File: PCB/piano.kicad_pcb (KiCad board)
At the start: 2 copper layers, 100 x 90 mm, 35 parts, among them J1 Conn_01x02, J2 Conn_01x04, J3 Conn_01x04, SW1 0, SW10 9, SW11 A, SW12 B, SW13 C, SW14 D, SW15 E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

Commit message: v0.2 PCB
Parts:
- added ?: , , F.Cu at (133.7, 64.2)
- added Q1: 2N3904, Package_TO_SOT_THT:TO-92_Inline, F.Cu at (169.4, 51.1)
- added R5: 10k, Resistor_THT:R_Axial_DIN0207_L6.3mm_D2.5mm_P10.16mm_Horizontal, F.Cu at (181.7, 34.6)
- added SW1: SW_SPDT_MSM, Suat:Schiebeschalter, F.Cu at (208.4, 34.0)
- added U2: LiPo_Module, Suat:LiPoChargerModule, F.Cu at (218.3, 49.0)
- BZ1: footprint Buzzer_Beeper:Buzzer_TDK_PS1240P02BT_D12.2mm_H6.5mm -> Suat:Buzzer_D12mm_Pins6mm
- D1, D2, D3, D4: footprint Diode_THT:D_A-405_P10.16mm_Horizontal -> Suat:D_A-405_P10.16mm_Horizontal
- J1: footprint Connector_JST:JST_EH_B2B-EH-A_1x02_P2.50mm_Vertical -> Connector_JST:JST_PH_B2B-PH-K_1x02_P2.00mm_Vertical
- J2, J3: footprint Connector_PinHeader_2.54mm:PinHeader_1x04_P2.54mm_Vertical -> Suat:PinHeader_1x04_P2.54mm_Vertical_Simple
- R1, R2, R3, R4: value R -> 10k
- SW-0: renamed from SW1; value 0 -> 0x0; footprint Button_Switch_THT:SW_PUSH_6mm -> Suat:SW_PUSH_6mm
- SW-1: renamed from SW2; value 1 -> 0x1; footprint Button_Switch_THT:SW_PUSH_6mm -> Suat:SW_PUSH_6mm
- SW-2: renamed from SW3; value 2 -> 0x2; footprint Button_Switch_THT:SW_PUSH_6mm -> Suat:SW_PUSH_6mm
- SW-3: renamed from SW4; value 3 -> 0x3; footprint Button_Switch_THT:SW_PUSH_6mm -> Suat:SW_PUSH_6mm
- SW-4: renamed from SW5; value 4 -> 0x4; footprint Button_Switch_THT:SW_PUSH_6mm -> Suat:SW_PUSH_6mm
- SW-5: renamed from SW6; value 5 -> 0x5; footprint Button_Switch_THT:SW_PUSH_6mm -> Suat:SW_PUSH_6mm
- SW-6: renamed from SW7; value 6 -> 0x6; footprint Button_Switch_THT:SW_PUSH_6mm -> Suat:SW_PUSH_6mm
- SW-7: renamed from SW8; value 7 -> 0x7; footprint Button_Switch_THT:SW_PUSH_6mm -> Suat:SW_PUSH_6mm
- SW-8: renamed from SW9; value 8 -> 0x8; footprint Button_Switch_THT:SW_PUSH_6mm -> Suat:SW_PUSH_6mm
- SW-9: renamed from SW10; value 9 -> 0x9; footprint Button_Switch_THT:SW_PUSH_6mm -> Suat:SW_PUSH_6mm
- SW-A1: renamed from SW11; value A -> 0xA; footprint Button_Switch_THT:SW_PUSH_6mm -> Suat:SW_PUSH_6mm
- SW-B1: renamed from SW12; value B -> 0xB; footprint Button_Switch_THT:SW_PUSH_6mm -> Suat:SW_PUSH_6mm
- SW-C1: renamed from SW13; value C -> 0xC; footprint Button_Switch_THT:SW_PUSH_6mm -> Suat:SW_PUSH_6mm
- SW-D1: renamed from SW14; value D -> 0xD; footprint Button_Switch_THT:SW_PUSH_6mm -> Suat:SW_PUSH_6mm
- SW-E1: renamed from SW15; value E -> 0xE3; footprint Button_Switch_THT:SW_PUSH_6mm -> Suat:SW_PUSH_6mm
- SW-F1: renamed from SW16; value F -> 0xF; footprint Button_Switch_THT:SW_PUSH_6mm -> Suat:SW_PUSH_6mm
- moved D1 65.5 mm to (214.6, 70.7)
- moved D2 47.5 mm to (206.2, 70.7)
- moved BZ1 39.0 mm to (170.0, 39.2)
- moved R4 37.3 mm to (154.3, 70.8), turned to -90 degrees
- moved D3 29.5 mm to (197.9, 70.7)
- moved R3 27.6 mm to (162.5, 70.8), turned to -90 degrees
- moved J1 26.5 mm to (217.0, 35.2)
- moved R2 19.7 mm to (170.7, 70.8), turned to -90 degrees
- moved R1 16.2 mm to (178.8, 70.8), turned to -90 degrees
- moved D4 11.6 mm to (189.5, 70.7)
- moved J2 9.96 mm to (198.2, 52.2), turned to -90 degrees
- moved J3 5.62 mm to (187.0, 40.7)
- moved SW-9 2.09 mm to (165.4, 100.0)
- moved SW-8 1.32 mm to (155.1, 100.0)
- moved SW-A1 1.23 mm to (185.6, 100.0)
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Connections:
- ? pad 1: (no net) -> GND (x4)
- BZ1 pad 1: Net-(BZ1-Pad1) -> Net-(SW1-Pad1)
- BZ1 pad 2: GND -> Net-(BZ1-Pad2)
- J1 pad 1: GND -> Net-(J1-Pad1)
- REF** pad 1: (no net) -> GND (x2)
- U1 pad 3: Net-(BZ1-Pad1) -> Net-(U1-Pad3)
- U1 pad 9: Net-(J1-Pad2) -> Net-(SW1-Pad1)
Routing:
- net Net-(SW1-Pad1): track 0.00 -> 80.1 mm
- net Net-(BZ1-Pad1): track 65.1 -> 0.00 mm
- net Net-(J1-Pad2): track 76.6 -> 18.7 mm
- net Net-(D2-Pad2): track 135.3 -> 181.1 mm, vias 1 -> 0
- net Net-(D1-Pad2): track 144.0 -> 183.9 mm
- net Net-(U1-Pad3): track 0.00 -> 32.7 mm
- net D8: track 213.5 -> 246.2 mm
- net Net-(Q1-Pad2): track 0.00 -> 31.4 mm
- net Net-(D3-Pad2): track 168.8 -> 197.4 mm
- net Net-(SW1-Pad2): track 0.00 -> 24.9 mm
- net GND: track 23.0 -> 0.00 mm, vias 7 -> 0
- net D7: track 200.3 -> 222.7 mm, vias 1 -> 0
- net Net-(J1-Pad1): track 0.00 -> 22.0 mm
- net Net-(BZ1-Pad2): track 0.00 -> 15.6 mm
- net D4: track 78.5 -> 92.3 mm, vias 1 -> 0
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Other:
- board text added: "+ -"
- board text added: "0 4 8 C 1 5 9 D 2 6 A E 3 7 B F"
- board text added: "Cols→"
- board text added: "Rows→"
- board text added: "v0.2 ://sui.li"
- board text removed: "+ - D0"
- board text removed: "F E D C B A 9 8 7 6 5 4 3 2 1 0"
- board text removed: "v0.1 ://sui.li"

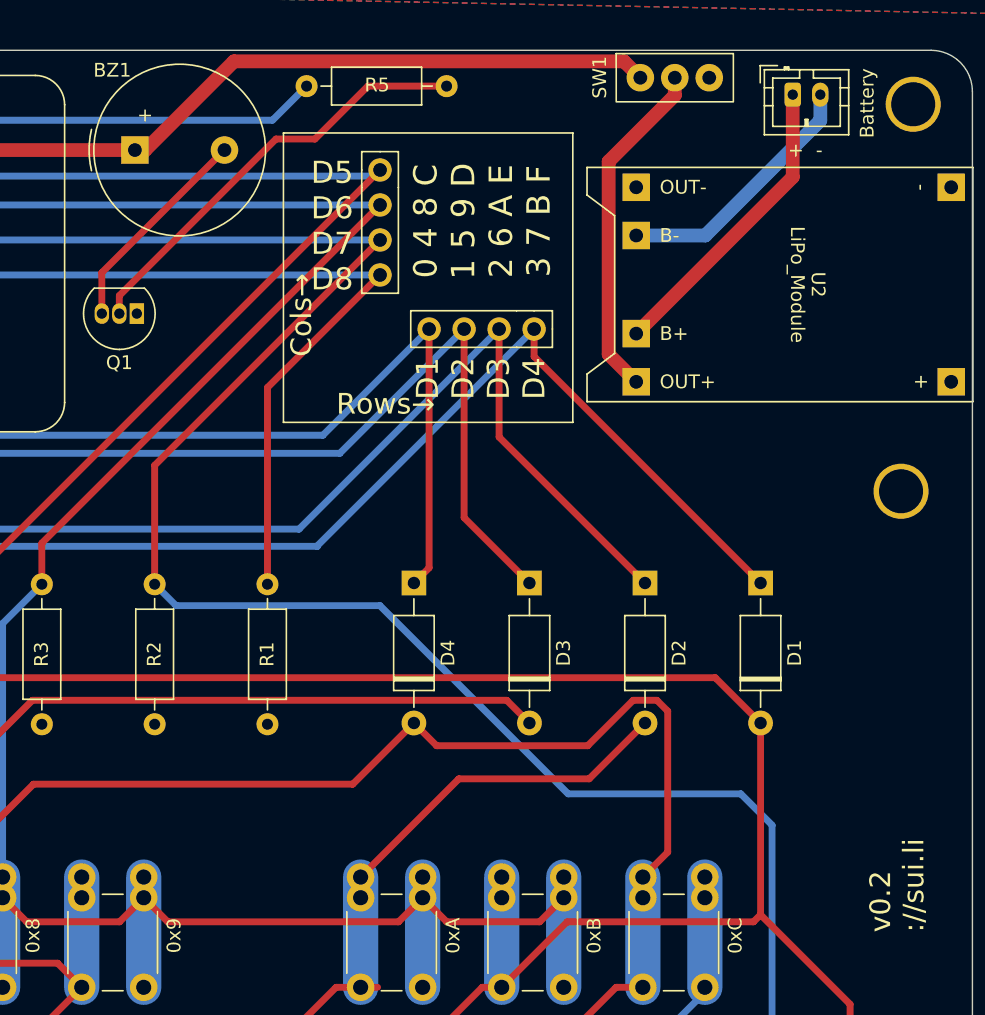
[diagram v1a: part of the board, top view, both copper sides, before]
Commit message: update pcb (larger footprint for transistor)
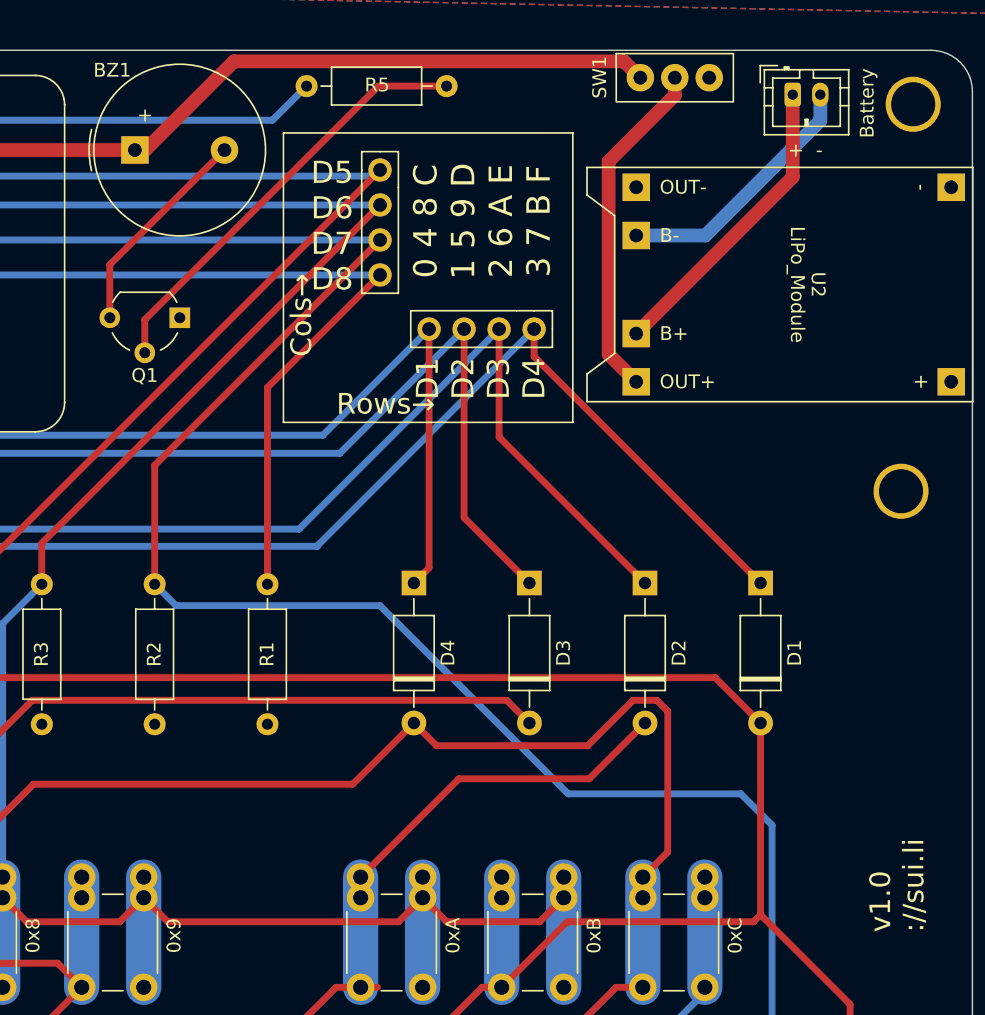
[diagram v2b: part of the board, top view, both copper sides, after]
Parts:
- Q1: footprint Package_TO_SOT_THT:TO-92_Inline -> Package_TO_SOT_THT:TO-92_Wide
- moved Q1 3.13 mm to (172.5, 51.4)
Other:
- board text added: "v1.0 ://sui.li"
- board text removed: "v0.2 ://sui.li"
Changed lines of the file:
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@@
     )
   )
-  (footprint "Package_TO_SOT_THT:TO-92_Inline" (layer "F.Cu")
-    (at 169.36 51.11 180)
-    (descr "TO-92 leads in-line, narrow, oval pads, drill 0.75mm (see NXP sot054_po.pdf)")
+  (footprint "Package_TO_SOT_THT:TO-92_Wide" (layer "F.Cu")
+    (at 172.48 51.41 180)
+    (descr "TO-92 leads molded, wide, drill 0.75mm (see NXP sot054_po.pdf)")
     (tags "to-92 sc-43 sc-43a sot54 PA33 transistor")
     (property "Sheetfile" "piano.kicad_sch")
     (property "Sheetname" "")
     (attr through_hole)
-    (fp_text reference "Q1" (at 1.27 -3.56) (layer "F.SilkS")
-      (effects (font (size 1 1) (thickness 0.15)))
-    )
-    (fp_text value "2N3904" (at 1.27 2.79) (layer "F.Fab")
-      (effects (font (size 1 1) (thickness 0.15)))
-    )
-    (fp_text user "${REFERENCE}" (at 1.27 0) (layer "F.Fab")
-      (effects (font (size 1 1) (thickness 0.15)))
-    )
-    (fp_line (start -0.53 1.85) (end 3.07 1.85) (layer "F.SilkS") (width 0.12))
-    (fp_arc (start -0.568478 1.838478) (mid -1.132087 -0.994977) (end 1.27 -2.6) (layer "F.SilkS") (width 0.12))
-    (fp_arc (start 1.27 -2.6) (mid 3.672087 -0.994977) (end 3.108478 1.838478) (layer "F.SilkS") (width 0.12))
-    (fp_line (start -1.46 -2.73) (end 4 -2.73) (layer "F.CrtYd") (width 0.05))
-    (fp_line (start -1.46 -2.73) (end -1.46 2.01) (layer "F.CrtYd") (width 0.05))
-    (fp_line (start 4 2.01) (end 4 -2.73) (layer "F.CrtYd") (width 0.05))
-    (fp_line (start 4 2.01) (end -1.46 2.01) (layer "F.CrtYd") (width 0.05))
-    (fp_line (start -0.5 1.75) (end 3 1.75) (layer "F.Fab") (width 0.1))
-    (fp_arc (start -0.483625 1.753625) (mid -1.021221 -0.949055) (end 1.27 -2.48) (layer "F.Fab") (width 0.1))
-    (fp_arc (start 1.27 -2.48) (mid 3.561221 -0.949055) (end 3.023625 1.753625) (layer "F.Fab") (width 0.1))
-    (pad "1" thru_hole rect (at 0 0 180) (size 1.05 1.5) (drill 0.75) (layers *.Cu *.Mask)
+    (fp_text reference "Q1" (at 2.55 -4.19 180) (layer "F.SilkS")
+      (effects (font (size 1 1) (thickness 0.15)))
+    )
+    (fp_text value "2N3904" (at 2.54 2.79 180) (layer "F.Fab")
+      (effects (font (size 1 1) (thickness 0.15)))
+    )
+    (fp_text user "${REFERENCE}" (at 2.54 0 180) (layer "F.Fab")
+      (effects (font (size 1 1) (thickness 0.15)))
+    )
+    (fp_line (start 0.74 1.85) (end 4.34 1.85) (layer "F.SilkS") (width 0.12))
+    (fp_arc (start 0.74 1.85) (mid 0.446097 1.509328) (end 0.215816 1.122795) (layer "F.SilkS") (width 0.12))
+    (fp_arc (start 4.864184 1.122795) (mid 4.633903 1.509328) (end 4.34 1.85) (layer "F.SilkS") (width 0.12))
+    (fp_arc (start 0.172801 -1.103842) (mid 0.678995 -1.832692) (end 1.4 -2.35) (layer "F.SilkS") (width 0.12))
+    (fp_arc (start 3.65 -2.35) (mid 4.382279 -1.833196) (end 4.895458 -1.098371) (layer "F.SilkS") (width 0.12))
+    (fp_line (start -1.01 -3.55) (end 6.09 -3.55) (layer "F.CrtYd") (width 0.05))
+    (fp_line (start 6.09 2.01) (end 6.09 -3.55) (layer "F.CrtYd") (width 0.05))
+    (fp_line (start 6.09 2.01) (end -1.01 2.01) (layer "F.CrtYd") (width 0.05))
+    (fp_line (start -1.01 -3.55) (end -1.01 2.01) (layer "F.CrtYd") (width 0.05))
+    (fp_line (start 0.8 1.75) (end 4.3 1.75) (layer "F.Fab") (width 0.1))
+    (fp_arc (start 0.786375 1.753625) (mid 0.248779 -0.949055) (end 2.54 -2.48) (layer "F.Fab") (width 0.1))
+    (fp_arc (start 2.54 -2.48) (mid 4.831221 -0.949055) (end 4.293625 1.753625) (layer "F.Fab") (width 0.1))
+    (pad "1" thru_hole rect (at 0 0 180) (size 1.5 1.5) (drill 0.8) (layers *.Cu *.Mask)
       (net 6 "GND") (pinfunction "E") (pintype "passive"))
-    (pad "2" thru_hole oval (at 1.27 0 180) (size 1.05 1.5) (drill 0.75) (layers *.Cu *.Mask)
+    (pad "2" thru_hole circle (at 2.54 -2.54 180) (size 1.5 1.5) (drill 0.8) (layers *.Cu *.Mask)
       (net 26 "Net-(Q1-Pad2)") (pinfunction "B") (pintype "passive"))
-    (pad "3" thru_hole oval (at 2.54 0 180) (size 1.05 1.5) (drill 0.75) (layers *.Cu *.Mask)
+    (pad "3" thru_hole circle (at 5.08 0 180) (size 1.5 1.5) (drill 0.8) (layers *.Cu *.Mask)
       (net 12 "Net-(BZ1-Pad2)") (pinfunction "C") (pintype "passive"))
-    (model "${KICAD6_3DMODEL_DIR}/Package_TO_SOT_THT.3dshapes/TO-92_Inline.wrl"
+    (model "${KICAD6_3DMODEL_DIR}/Package_TO_SOT_THT.3dshapes/TO-92_Wide.wrl"
       (offset (xyz 0 0 0))
       (scale (xyz 1 1 1))
@@
     (effects (font (size 1 1) (thickness 0.15)))
   )
-  (gr_text "v0.2\n://sui.li" (at 224.536 96.012 90) (layer "F.SilkS")
+  (gr_text "v1.0\n://sui.li" (at 224.536 96.012 90) (layer "F.SilkS")
     (effects (font (size 1.5 1.5) (thickness 0.3)) (justify left))
   )
@@
   (segment (start 152.44952 59.93452) (end 150.7 58.185) (width 0.5) (layer "B.Cu") (net 9))
   (segment (start 190.57 52.23) (end 182.86548 59.93452) (width 0.5) (layer "B.Cu") (net 9))
-  (segment (start 175.72 39.24) (end 166.82 48.14) (width 0.5) (layer "F.Cu") (net 12))
-  (segment (start 166.82 48.14) (end 166.82 51.11) (width 0.5) (layer "F.Cu") (net 12))
+  (segment (start 167.4 47.56) (end 175.72 39.24) (width 0.5) (layer "F.Cu") (net 12))
+  (segment (start 167.4 51.41) (end 167.4 47.56) (width 0.5) (layer "F.Cu") (net 12))
   (segment (start 200.590489 95.249511) (end 195.84 100) (width 0.5) (layer "F.Cu") (net 16))
   (segment (start 143.61951 77.53049) (end 140.56 80.59) (width 0.5) (layer "F.Cu") (net 16))
@@
   (segment (start 169.97 39.24) (end 176.409511 32.800489) (width 1) (layer "F.Cu") (net 24))
   (segment (start 154.945 39.24) (end 138 56.185) (width 1) (layer "F.Cu") (net 24))
-  (segment (start 186.13 34.6) (end 191.84 34.6) (width 0.5) (layer "F.Cu") (net 26))
-  (segment (start 182.29 38.44) (end 186.13 34.6) (width 0.5) (layer "F.Cu") (net 26))
-  (segment (start 179.455978 38.44) (end 182.29 38.44) (width 0.5) (layer "F.Cu") (net 26))
-  (segment (start 168.09 49.805978) (end 179.455978 38.44) (width 0.5) (layer "F.Cu") (net 26))
-  (segment (start 168.09 51.11) (end 168.09 49.805978) (width 0.5) (layer "F.Cu") (net 26))
+  (segment (start 186.890978 34.6) (end 191.84 34.6) (width 0.5) (layer "F.Cu") (net 26))
+  (segment (start 169.94 53.95) (end 169.94 51.550978) (width 0.5) (layer "F.Cu") (net 26))
+  (segment (start 169.94 51.550978) (end 186.890978 34.6) (width 0.5) (layer "F.Cu") (net 26))
   (segment (start 150.7 35.325) (end 152.449511 37.074511) (width 0.5) (layer "B.Cu") (net 27))
   (segment (start 152.449511 37.074511) (end 179.205489 37.074511) (width 0.5) (layer "B.Cu") (net 27))
